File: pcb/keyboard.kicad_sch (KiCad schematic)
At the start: 29 parts

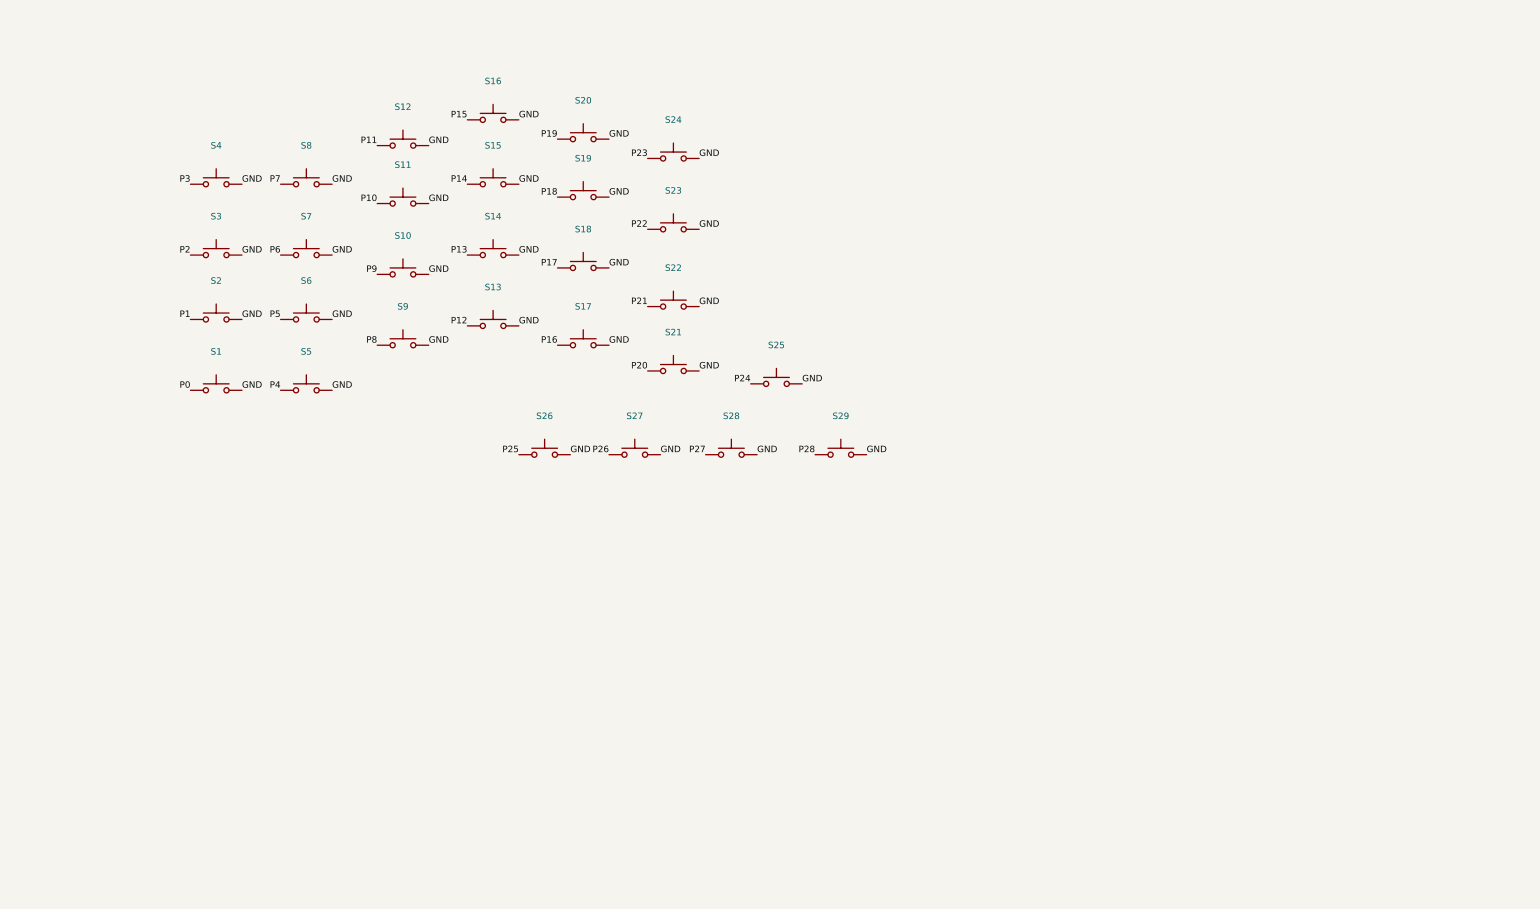
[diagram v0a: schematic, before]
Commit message: #1 add battery management and USB socket schematics
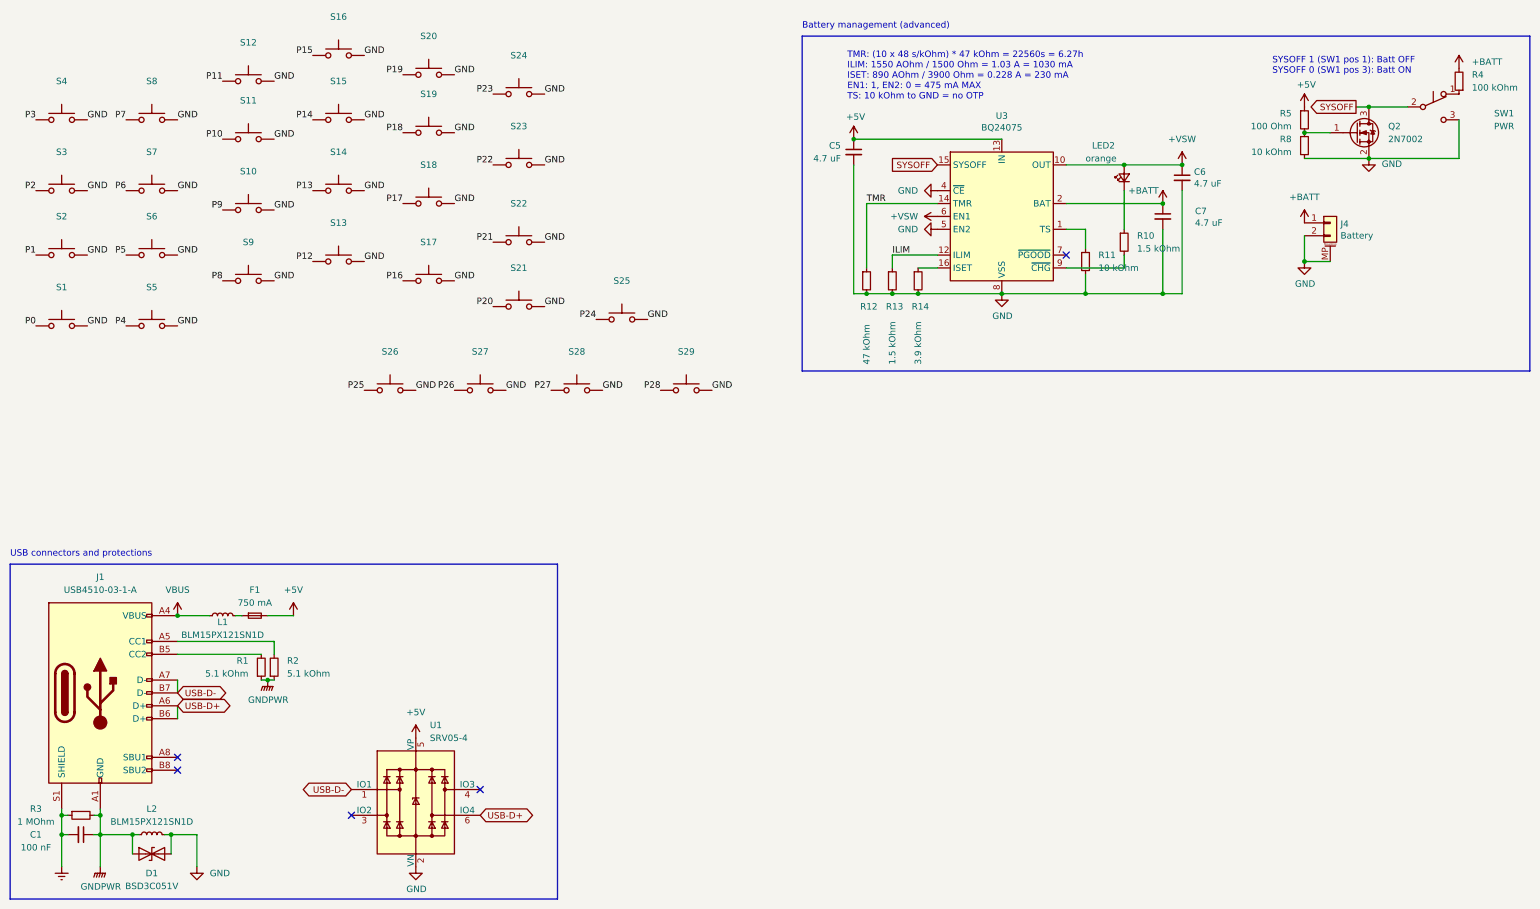
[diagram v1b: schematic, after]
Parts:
- added C1: 100 nF, Capacitor_SMD:C_0402_1005Metric, symbol Device:C_Small
- added C5, C6, C7: 4.7 uF, Capacitor_SMD:C_0402_1005Metric, symbol Device:C_Small
- added D1: BSD3C051V, Diode_SMD:D_SOD-323, symbol Device:D_TVS
- added F1: 750 mA, Fuse:Fuse_0603_1608Metric, symbol Device:Fuse_Small
- added J1: USB4510-03-1-A, Connector_USB:USB_C_Receptacle_HRO_TYPE-C-31-M-12, symbol Connector:USB_C_Receptacle_USB2.0
- added J4: Battery, Connector_JST:JST_PH_S2B-PH-K_1x02_P2.00mm_Horizontal, symbol Connector_Generic_MountingPin:Conn_01x02_MountingPin
- added L1, L2: BLM15PX121SN1D, Inductor_SMD:L_0402_1005Metric, symbol Device:L_Small
- added LED2: orange, LED_SMD:LED_0402_1005Metric, symbol Device:LED_Small
- added Q2: 2N7002, Package_TO_SOT_SMD:SOT-23, symbol Transistor_FET:2N7002
- added R1, R2: 5.1 kOhm, Resistor_SMD:R_0402_1005Metric, symbol Device:R_Small
- added R10, R13: 1.5 kOhm, Resistor_SMD:R_0402_1005Metric, symbol Device:R_Small
- added R11, R8: 10 kOhm, Resistor_SMD:R_0402_1005Metric, symbol Device:R_Small
- added R12: 47 kOhm, Resistor_SMD:R_0402_1005Metric, symbol Device:R_Small
- added R14: 3.9 kOhm, Resistor_SMD:R_0402_1005Metric, symbol Device:R_Small
- added R3: 1 MOhm, Resistor_SMD:R_0402_1005Metric, symbol Device:R_Small
- added R4: 100 kOhm, Resistor_SMD:R_0402_1005Metric, symbol Device:R_Small
- added R5: 100 Ohm, Resistor_SMD:R_0402_1005Metric, symbol Device:R_Small
- added SW1: PWR, PCM_marbastlib-various:SW_MSK12C02-HB, symbol Switch:SW_Push_SPDT
- added U1: SRV05-4, Package_TO_SOT_SMD:SOT-23-6, symbol Power_Protection:SRV05-4
- added U3: BQ24075, Package_DFN_QFN:VQFN-16-1EP_3x3mm_P0.5mm_EP1.6x1.6mm, symbol Battery_Management:BQ24075RGT
- S1, S10, S11, S12, S13, S14, S15, S16, S17, S18, S19, S2, S20, S21, S22, S23, S24, S25, S26, S27, S28, S29, S3, S4, S5, S6, S7, S8, S9: footprint kali_choc_v1:Kailh_socket_PG1350_optional -> keyboard:Kailh_socket_PG1350_optional
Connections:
- net GND: now also C5.2, C6.2, C7.2, D1.2 (A2), J4.2 (Pin_2), J4.MP (MountPin), L2.2, Q2.2 (S), R11.2, R12.2, R13.2, R14.2, R8.2, SW1.3 (C), U1.2 (VN), U3.17 (VSS), U3.4 (~{CE}), U3.5 (EN2), U3.8 (VSS)
- new net: LED2.1 (K), R10.1
- new net: R10.2, U3.9 (~{CHG})
- new net: R14.1, U3.16 (ISET)
- new net: J1.B5 (CC2), R1.2
- new net: Q2.1 (G), R5.2, R8.1
- new net: F1.1, L1.2
- new net: R11.1, U3.1 (TS)
- new net: R4.1, SW1.1 (A)
- new net: J1.A5 (CC1), R2.2
- new net +5V: C5.1, F1.2, R5.1, U1.5 (VP), U3.13 (IN)
- new net +BATT: C7.1, J4.1 (Pin_1), R4.2, U3.2 (BAT), U3.3 (BAT)
- new net +VSW: C6.1, LED2.2 (A), U3.10 (OUT), U3.11 (OUT), U3.6 (EN1)
- new net Earth: C1.2, J1.S1 (SHIELD), R3.1
- new net GNDPWR: C1.1, D1.1 (A1), J1.A1 (GND), J1.A12 (GND), J1.B1 (GND), J1.B12 (GND), L2.1, R1.1, R2.1, R3.2
- new net ILIM: R13.1, U3.12 (ILIM)
- new net SYSOFF: Q2.3 (D), SW1.2 (B), U3.15 (SYSOFF)
- new net TMR: R12.1, U3.14 (TMR)
- new net USB-D+: J1.A6 (D+), J1.B6 (D+), U1.6 (IO4)
- new net USB-D-: J1.A7 (D-), J1.B7 (D-), U1.1 (IO1)
- new net VBUS: J1.A4 (VBUS), J1.A9 (VBUS), J1.B4 (VBUS), J1.B9 (VBUS), L1.1
- no-connect marks 0 -> 5
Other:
- note added: "Battery management (advanced)"
- note added: "SYSOFF 1 (SW1 pos 1): Batt OFF SYSOFF 0 (SW1 pos 3): Batt ON"
- note added: "TMR: (10 x 48 s/kOhm) * 47 kOhm = 22560s = 6.27h ILIM: 1550 AOhm / 1500 Ohm = 1.03 A = 1030 mA ISET: 890 AOhm / 3900 Ohm = 0.228 A = 230 mA EN1: 1, EN2: 0 = 475 mA MAX TS: 10 kOhm to GND = no OTP"
- note added: "USB connectors and protections"
- moved on the sheet: S1, S10, S11, S12, S13, S14, S15, S16, S17, S18, S19, S2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
